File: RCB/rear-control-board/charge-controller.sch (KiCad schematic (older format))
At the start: 0 parts

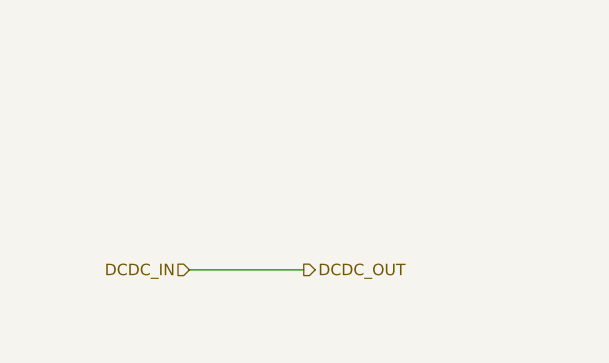
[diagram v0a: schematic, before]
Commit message: finish schematic, start layout
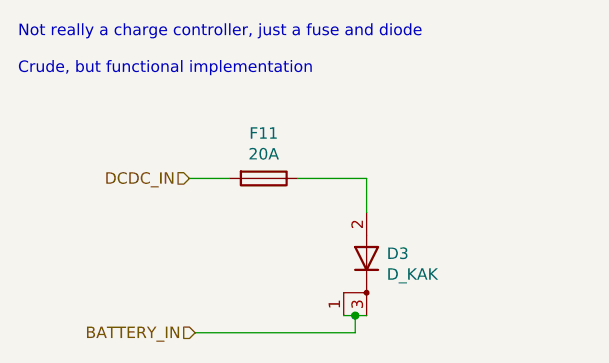
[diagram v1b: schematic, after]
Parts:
- added D3: D_KAK, symbol Device:D_KAK
- added F11: 20A, AERO_Footprints:Fuseholder_Blade_Mini_Keystone_3568, symbol Device:Fuse
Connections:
- net DCDC_IN: now also F11.2
- new net: D3.2 (A), F11.1
- new net BATTERY_IN: D3.1 (K), D3.3 (K)
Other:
- note added: "Not really a charge controller, just a fuse and diode\n\nCrude, but functional implementation"
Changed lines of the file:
@@
 $Descr A4 11693 8268
 encoding utf-8
-Sheet 2 6
+Sheet 2 5
 Title ""
 Date ""
@@
 Comment4 ""
 $EndDescr
-Text HLabel 3900 3650 0    50   Input ~ 0
+Text HLabel 3900 3250 0    50   Input ~ 0
 DCDC_IN
-Text HLabel 4400 3650 2    50   Output ~ 0
-DCDC_OUT
+Text HLabel 3925 3925 0    50   Input ~ 0
+BATTERY_IN
+$Comp
+L Device:Fuse F11
+U 1 1 622D3615
+P 4225 3250
+F 0 "F11" V 4028 3250 50  0000 C CNN
+F 1 "20A" V 4119 3250 50  0000 C CNN
+F 2 "AERO_Footprints:Fuseholder_Blade_Mini_Keystone_3568" V 4155 3250 50  0001 C CNN
+F 3 "~" H 4225 3250 50  0001 C CNN
+	1    4225 3250
+	0    1    1    0
+$EndComp
 Wire Wire Line
-	4400 3650 3900 3650
+	3900 3250 4075 3250
+Wire Wire Line
+	4375 3250 4675 3250
+Wire Wire Line
+	4675 3250 4675 3400
+Text Notes 3150 2800 0    50   ~ 0
+Not really a charge controller, just a fuse and diode\n\nCrude, but functional implementation
+Wire Wire Line
+	4625 3850 4625 3925
+Wire Wire Line
+	4625 3925 3925 3925
+$Comp
+L Device:D_KAK D3
+U 1 1 6256B1F2
+P 4675 3600
+F 0 "D3" V 4696 3512 50  0000 R CNN
+F 1 "D_KAK" V 4605 3512 50  0000 R CNN
+F 2 "" H 4675 3600 50  0001 C CNN
+F 3 "~" H 4675 3600 50  0001 C CNN
+	1    4675 3600
+	0    -1   -1   0
+$EndComp
+Wire Wire Line
+	4575 3850 4625 3850
+Wire Wire Line
+	4675 3850 4625 3850
+Connection ~ 4625 3850
 $EndSCHEMATC

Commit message: working on layout
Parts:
- D3: footprint (none) -> Package_TO_SOT_SMD:TO-252-2
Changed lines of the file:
@@
 F 0 "D3" V 4696 3512 50  0000 R CNN
 F 1 "D_KAK" V 4605 3512 50  0000 R CNN
-F 2 "" H 4675 3600 50  0001 C CNN
+F 2 "Package_TO_SOT_SMD:TO-252-2" H 4675 3600 50  0001 C CNN
 F 3 "~" H 4675 3600 50  0001 C CNN
 	1    4675 3600
